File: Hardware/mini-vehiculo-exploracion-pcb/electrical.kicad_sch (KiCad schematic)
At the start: 21 parts, among them IC2 TPS564257DRLR

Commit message: actualizacion labels pcb drivers
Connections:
- net +5V renamed V_BUS
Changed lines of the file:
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@@
-	(wire
-		(pts
-			(xy 52.07 105.41) (xy 52.07 123.19)
-		)
-		(stroke
-			(width 0)
-			(type default)
-		)
-	)
 	(wire
 		(pts
@@
 	(wire
 		(pts
+			(xy 52.07 104.14) (xy 52.07 123.19)
+		)
+		(stroke
+			(width 0)
+			(type default)
+		)
+	)
+	(wire
+		(pts
 			(xy 165.1 54.61) (xy 176.53 54.61)
 		)
@@
 			(width 0)
 			(type default)
+		)
+	)
+	(global_label "V_BUS"
+		(shape input)
+		(at 52.07 104.14 0)
+		(fields_autoplaced yes)
+		(effects
+			(font
+				(size 1.27 1.27)
+			)
+			(justify left)
+		)
+		(property "Intersheetrefs" "${INTERSHEET_REFS}"
+			(at 60.9214 104.14 0)
+			(effects
+				(font
+					(size 1.27 1.27)
+				)
+				(justify left)
+				(hide yes)
+			)
 		)
 	)
@@
 					(unit 1)
 				)
-			)
-		)
-	)
-	(symbol
-		(lib_id "power:+5V")
-		(at 52.07 105.41 0)
-		(unit 1)
-		(exclude_from_sim no)
-		(in_bom yes)
-		(on_board yes)
-		(dnp no)
-		(fields_autoplaced yes)
-		(property "Reference" "#PWR024"
-			(at 52.07 109.22 0)
-			(effects
-				(font
-					(size 1.27 1.27)
-				)
-				(hide yes)
-			)
-		)
-		(property "Value" "+5V"
-			(at 52.07 100.33 0)
-			(effects
-				(font
-					(size 1.27 1.27)
-				)
-			)
-		)
-		(property "Footprint" ""
-			(at 52.07 105.41 0)
-			(effects
-				(font
-					(size 1.27 1.27)
-				)
-				(hide yes)
-			)
-		)
-		(property "Datasheet" ""
-			(at 52.07 105.41 0)
-			(effects
-				(font
-					(size 1.27 1.27)
-				)
-				(hide yes)
-			)
-		)
-		(property "Description" "Power symbol creates a global label with name \"+5V\""
-			(at 52.07 105.41 0)
-			(effects
-				(font
-					(size 1.27 1.27)
-				)
-				(hide yes)
-			)
-		)
-		(pin "1"
-		)
-		(instances
-			(project "mini-vehiculo-exploracion-pcb"
-				(path "/3cb3b833-c38f-47b4-b7e9-f0e6337b7613/d054e30f-93c7-4141-9b1f-3289ce35fefa"
-					(reference "#PWR024")
-					(unit 1)
-				)

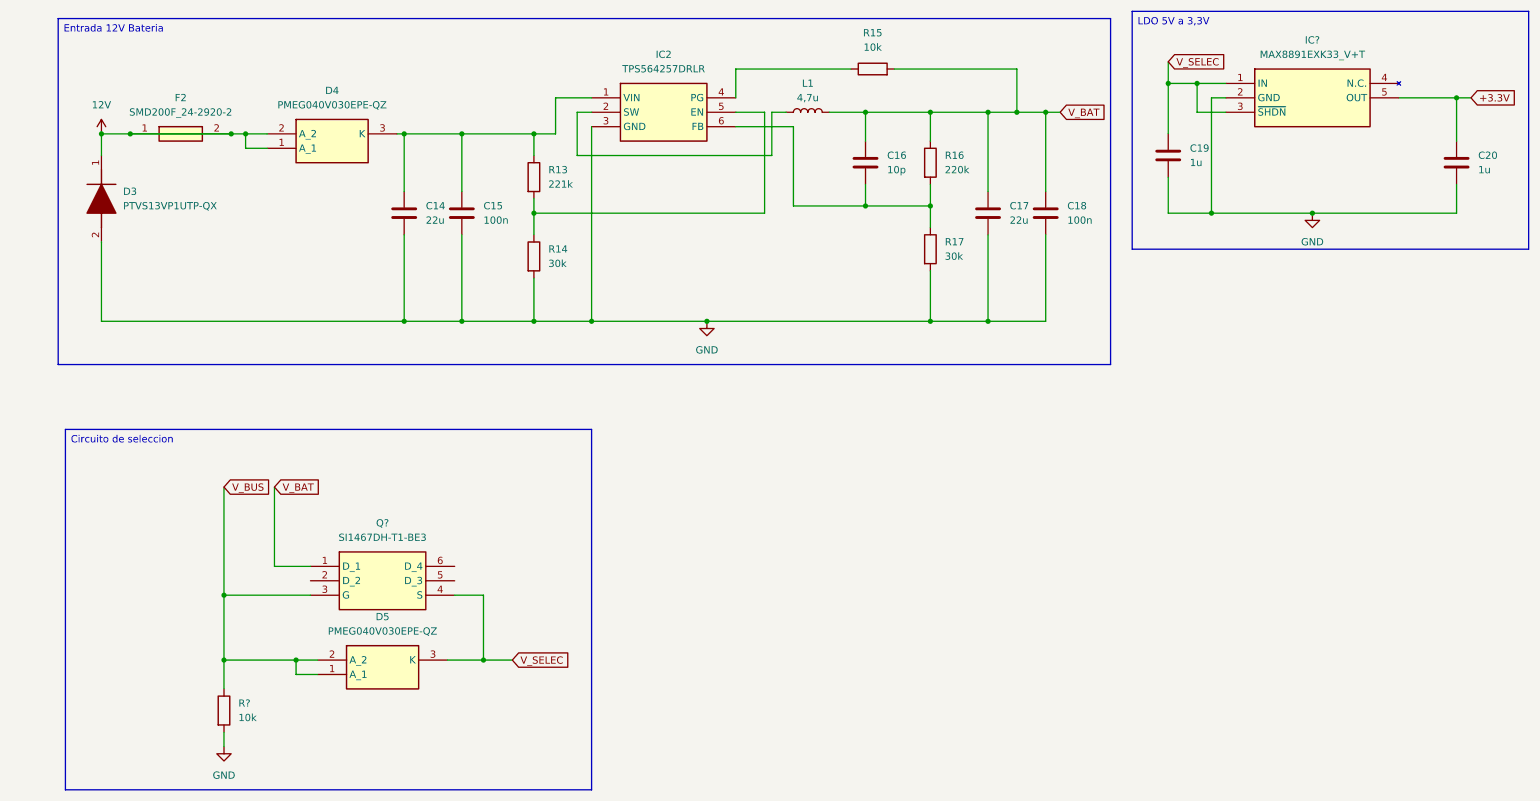
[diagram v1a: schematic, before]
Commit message: Add pin headers, run ERC
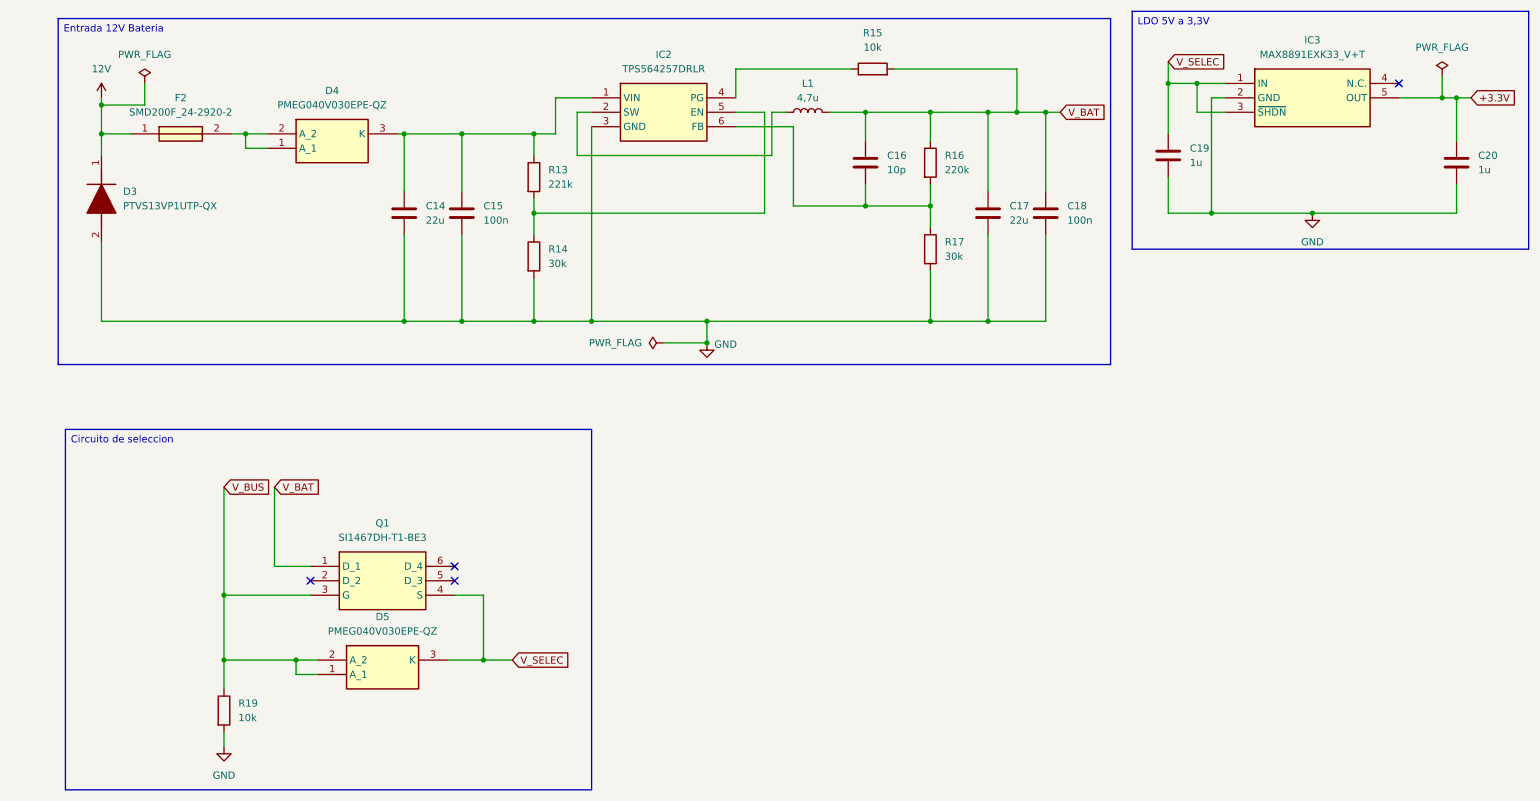
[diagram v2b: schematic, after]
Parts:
- removed R?: 10k, symbol Device:R
- added R19: 10k, symbol Device:R
- gave numbers to parts that had none: 2
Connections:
- net 12V: no longer D4.1 (A_1), D4.2 (A_2), F2.2
- net GND: now also R19.2
- net V_BUS: now also R19.1
- new net: D4.1 (A_1), D4.2 (A_2), F2.2
- no-connect marks 0 -> 4

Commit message: Assigned NET CLASSES
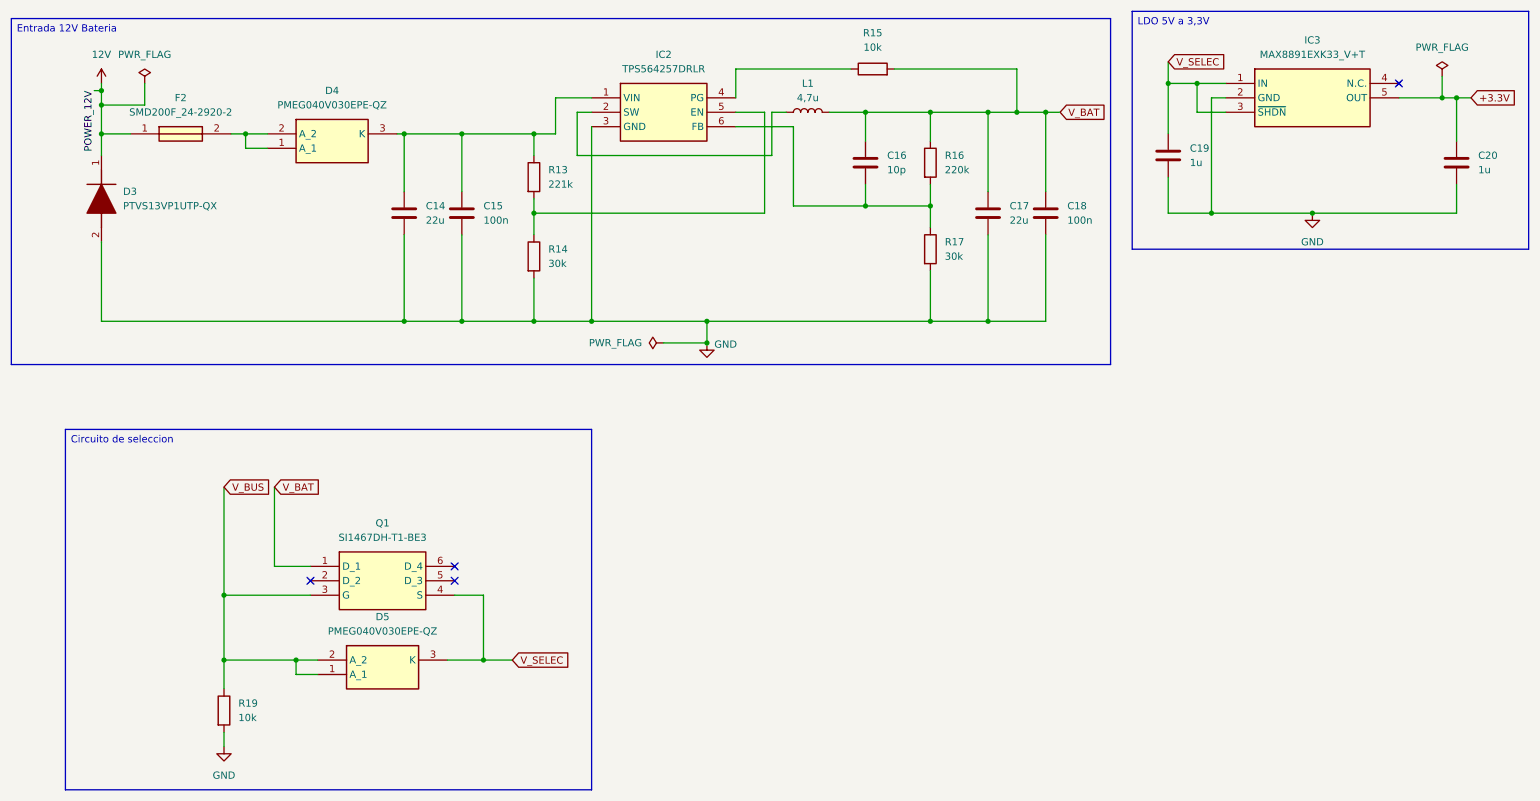
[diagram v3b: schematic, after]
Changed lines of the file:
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@@
 	(text_box "Entrada 12V Bateria\n"
 		(exclude_from_sim no)
-		(at 22.86 21.59 0)
-		(size 185.42 60.96)
+		(at 14.605 21.59 0)
+		(size 193.675 60.96)
 		(margins 0.9525 0.9525 0.9525 0.9525)
 		(stroke
@@
 	)
 	(junction
+		(at 30.48 34.29)
+		(diameter 0)
+		(color 0 0 0 0)
+	)
+	(junction
 		(at 165.1 38.1)
 		(diameter 0)
@@
 	(wire
 		(pts
+			(xy 30.48 34.29) (xy 30.48 36.83)
+		)
+		(stroke
+			(width 0)
+			(type default)
+		)
+	)
+	(wire
+		(pts
 			(xy 83.82 52.07) (xy 83.82 41.91)
 		)
@@
 	(wire
 		(pts
-			(xy 30.48 35.56) (xy 30.48 36.83)
+			(xy 30.48 33.02) (xy 30.48 34.29)
 		)
 		(stroke
@@
 	(wire
 		(pts
+			(xy 29.21 34.29) (xy 30.48 34.29)
+		)
+		(stroke
+			(width 0)
+			(type default)
+		)
+	)
+	(wire
+		(pts
 			(xy 269.24 35.56) (xy 271.78 35.56)
 		)
@@
 		)
 	)
+	(label "POWER_12V"
+		(at 29.21 34.29 270)
+		(effects
+			(font
+				(size 1.27 1.27)
+			)
+			(justify right bottom)
+		)
+	)
 	(global_label "V_BUS"
 		(shape input)
@@
 	(symbol
 		(lib_id "power:VDC")
-		(at 30.48 35.56 0)
+		(at 30.48 33.02 0)
 		(unit 1)
 		(exclude_from_sim no)
@@
 		(fields_autoplaced yes)
 		(property "Reference" "#PWR023"
-			(at 30.48 39.37 0)
+			(at 30.48 36.83 0)
 			(effects
 				(font
@@
 		)
 		(property "Value" "12V"
-			(at 30.48 30.48 0)
+			(at 30.48 27.94 0)
 			(effects
 				(font
@@
 		)
 		(property "Footprint" ""
-			(at 30.48 35.56 0)
+			(at 30.48 33.02 0)
 			(effects
 				(font
@@
 		)
 		(property "Datasheet" ""
-			(at 30.48 35.56 0)
+			(at 30.48 33.02 0)
 			(effects
 				(font
@@
 		)
 		(property "Description" "Power symbol creates a global label with name \"VDC\""
-			(at 30.48 35.56 0)
+			(at 30.48 33.02 0)
 			(effects
 				(font

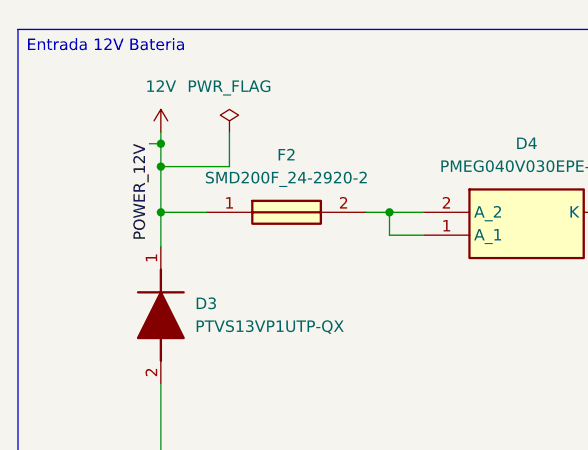
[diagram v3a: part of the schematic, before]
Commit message: Add battery sensor
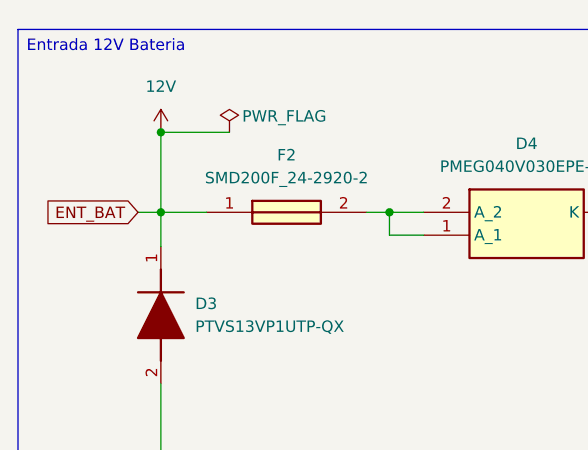
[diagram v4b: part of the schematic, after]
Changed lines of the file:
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@@
-	)
-	(junction
-		(at 30.48 34.29)
-		(diameter 0)
-		(color 0 0 0 0)
 	)
 	(junction
@@
 	)
 	(junction
-		(at 30.48 36.83)
+		(at 30.48 33.02)
 		(diameter 0)
 		(color 0 0 0 0)
@@
 	(wire
 		(pts
-			(xy 30.48 34.29) (xy 30.48 36.83)
-		)
-		(stroke
-			(width 0)
-			(type default)
-		)
-	)
-	(wire
-		(pts
 			(xy 83.82 52.07) (xy 83.82 41.91)
 		)
@@
 	(wire
 		(pts
-			(xy 38.1 33.02) (xy 38.1 36.83)
-		)
-		(stroke
-			(width 0)
-			(type default)
-		)
-	)
-	(wire
-		(pts
 			(xy 196.85 74.93) (xy 186.69 74.93)
 		)
@@
 	(wire
 		(pts
+			(xy 27.94 41.91) (xy 30.48 41.91)
+		)
+		(stroke
+			(width 0)
+			(type default)
+		)
+	)
+	(wire
+		(pts
 			(xy 110.49 41.91) (xy 106.68 41.91)
 		)
@@
 	(wire
 		(pts
-			(xy 30.48 33.02) (xy 30.48 34.29)
-		)
-		(stroke
-			(width 0)
-			(type default)
-		)
-	)
-	(wire
-		(pts
 			(xy 147.32 55.88) (xy 106.68 55.88)
 		)
@@
 	(wire
 		(pts
-			(xy 30.48 36.83) (xy 30.48 41.91)
-		)
-		(stroke
-			(width 0)
-			(type default)
-		)
-	)
-	(wire
-		(pts
 			(xy 176.53 54.61) (xy 176.53 58.42)
 		)
@@
 	(wire
 		(pts
-			(xy 29.21 34.29) (xy 30.48 34.29)
-		)
-		(stroke
-			(width 0)
-			(type default)
-		)
-	)
-	(wire
-		(pts
 			(xy 269.24 35.56) (xy 271.78 35.56)
 		)
@@
 	(wire
 		(pts
-			(xy 30.48 36.83) (xy 38.1 36.83)
+			(xy 30.48 33.02) (xy 38.1 33.02)
 		)
 		(stroke
@@
 		)
 	)
-	(label "POWER_12V"
-		(at 29.21 34.29 270)
-		(effects
-			(font
-				(size 1.27 1.27)
-			)
-			(justify right bottom)
+	(wire
+		(pts
+			(xy 30.48 33.02) (xy 30.48 41.91)
+		)
+		(stroke
+			(width 0)
+			(type default)
 		)
 	)
@@
 				)
 				(justify left)
+				(hide yes)
+			)
+		)
+	)
+	(global_label "ENT_BAT"
+		(shape input)
+		(at 27.94 41.91 180)
+		(fields_autoplaced yes)
+		(effects
+			(font
+				(size 1.27 1.27)
+			)
+			(justify right)
+		)
+		(property "Intersheetrefs" "${INTERSHEET_REFS}"
+			(at 17.2139 41.91 0)
+			(effects
+				(font
+					(size 1.27 1.27)
+				)
+				(justify right)
 				(hide yes)
 			)
@@
 		(on_board yes)
 		(dnp no)
-		(fields_autoplaced yes)
 		(property "Reference" "#FLG01"
 			(at 38.1 31.115 0)
@@
 		)
 		(property "Value" "PWR_FLAG"
-			(at 38.1 27.94 0)
-			(effects
-				(font
+			(at 44.196 31.242 0)
+			(effects
+				(font

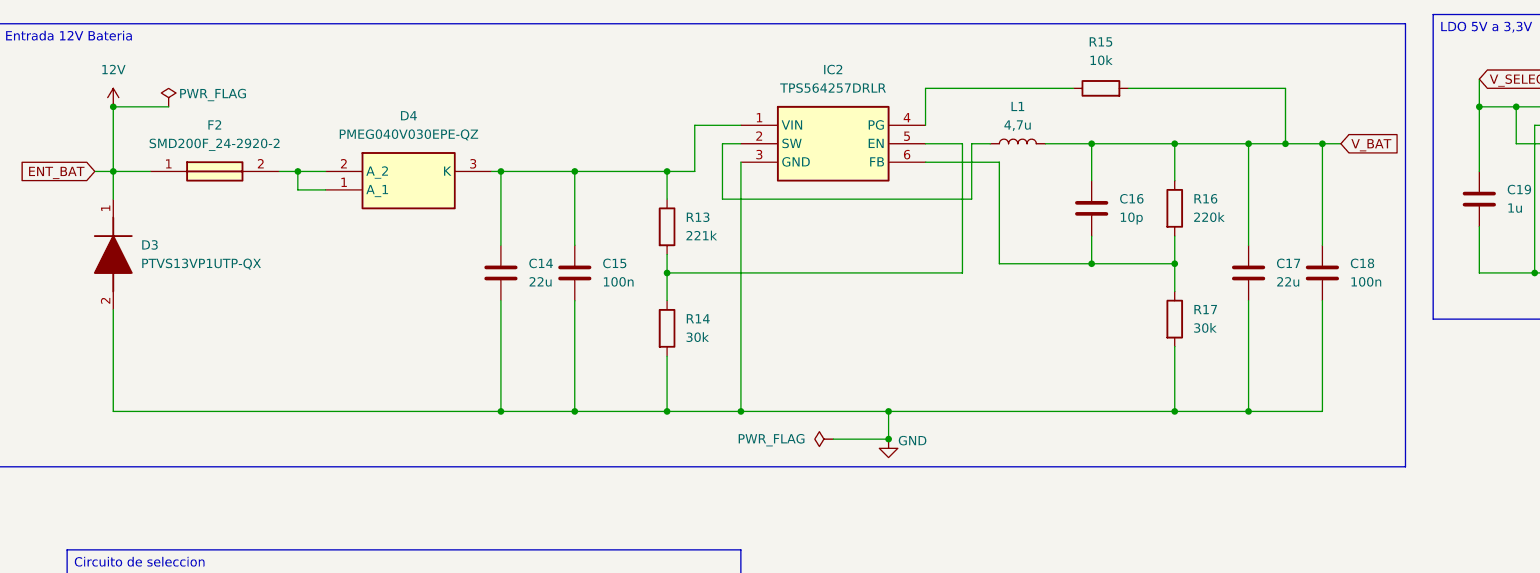
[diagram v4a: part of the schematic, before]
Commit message: cambio circuito 5V pcb control
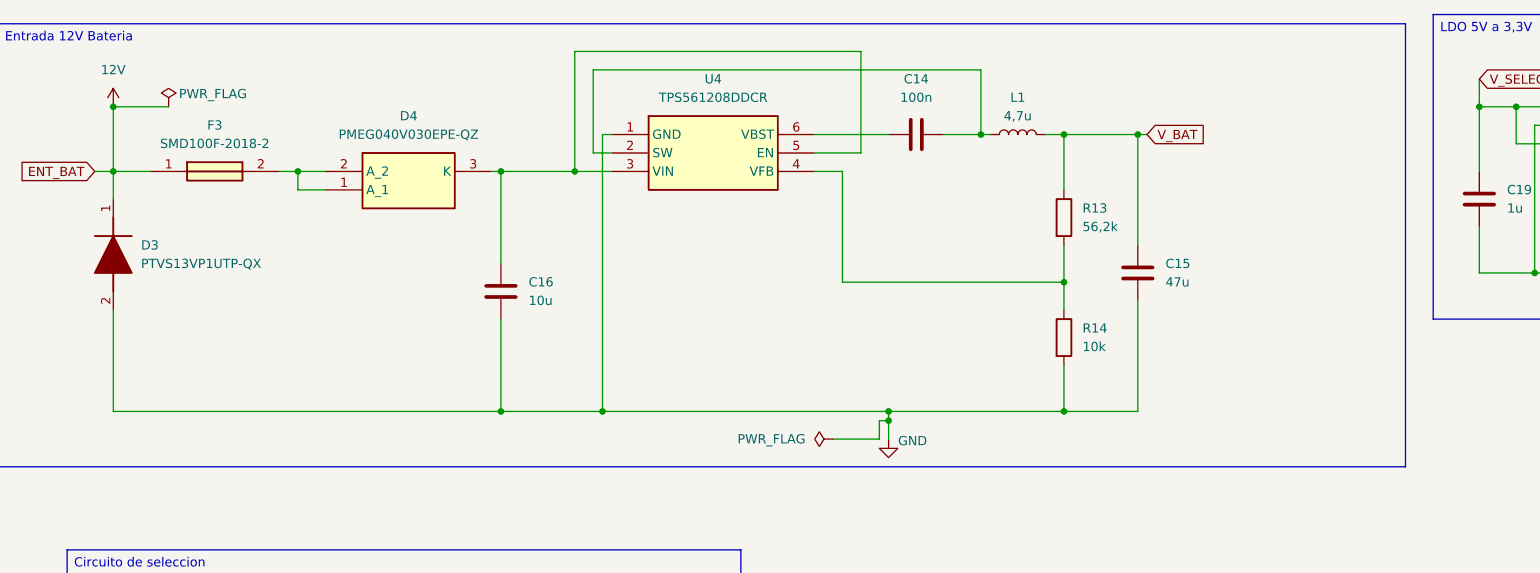
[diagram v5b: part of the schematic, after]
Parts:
- removed C17: 22u, symbol Device:C
- removed C18: 100n, symbol Device:C
- removed F2: SMD200F_24-2920-2, SMD200F2429202, symbol SMD200F_24-2920-2:SMD200F_24-2920-2
- removed IC2: TPS564257DRLR, SOTFL50P160X60-6N, symbol SamacSys_Parts:TPS564257DRLR
- removed R15: 10k, symbol Device:R
- removed R16: 220k, symbol Device:R
- removed R17: 30k, symbol Device:R
- added F3: SMD100F-2018-2, SMD030F20182, symbol SMD100F-2018-2:SMD100F-2018-2
- added U4: TPS561208DDCR, SOT95P280X110-6N, symbol TPS561208DDCR:TPS561208DDCR
- C14: value 22u -> 100n
- C15: value 100n -> 47u
- C16: value 10p -> 10u
- R13: value 221k -> 56,2k
- R14: value 30k -> 10k
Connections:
- net 12V: now also F3.1
- net GND: now also C16.2, U4.1 (GND); no longer C14.2
- net V_BAT: now also C15.1, R13.1; no longer C16.1
- net at L1.1: now also C14.2, U4.2 (SW)
- net at D4.1 (A_1), D4.2 (A_2): now also F3.2
- net at R13.2, R14.1: now also U4.4 (VFB)
- new net: C16.1, D4.3 (K), U4.3 (VIN), U4.5 (EN)
- new net: C14.1, U4.6 (VBST)

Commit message: Add footprints
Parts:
- C14, C15, C16, C19, C20: footprint (none) -> Capacitor_SMD:C_0805_2012Metric_Pad1.18x1.45mm_HandSolder
- D3: footprint SODFL4725X110N -> PTVS13VP1UTP-QX:SODFL4725X110N
- D4, D5: footprint PMEG040V030EPEQZ -> PMEG040V030EPE-QZ:PMEG040V030EPEQZ
- F3: footprint SMD030F20182 -> SMD100F-2018-2:SMD030F20182
- IC3: footprint SOT65P210X110-5N -> MAX8891EXK33_V+T:SOT65P210X110-5N
- Q1: footprint SOT65P210X110-6N -> SI1467DH-T1-BE3:SOT65P210X110-6N
- R13, R14, R19: footprint (none) -> Resistor_SMD:R_0805_2012Metric_Pad1.20x1.40mm_HandSolder
- U4: footprint SOT95P280X110-6N -> TPS561208DDCR:SOT95P280X110-6N
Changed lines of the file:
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@@
 			)
 		)
-		(property "Footprint" ""
+		(property "Footprint" "Capacitor_SMD:C_0805_2012Metric_Pad1.18x1.45mm_HandSolder"
 			(at 84.7852 62.23 0)
 			(effects
@@
 			)
 		)
-		(property "Footprint" ""
+		(property "Footprint" "Capacitor_SMD:C_0805_2012Metric_Pad1.18x1.45mm_HandSolder"
 			(at 219.4052 49.53 0)
 			(effects
@@
 			)
 		)
-		(property "Footprint" "SOT65P210X110-5N"
+		(property "Footprint" "MAX8891EXK33_V+T:SOT65P210X110-5N"
 			(at 255.27 127.94 0)
 			(effects
@@
 			)
 		)
-		(property "Footprint" "SOT95P280X110-6N"
+		(property "Footprint" "TPS561208DDCR:SOT95P280X110-6N"
 			(at 123.19 131.75 0)
 			(effects
@@
 			)
 		)
-		(property "Footprint" "PMEG040V030EPEQZ"
+		(property "Footprint" "PMEG040V030EPE-QZ:PMEG040V030EPEQZ"
 			(at 78.74 136.83 0)
 			(effects
@@
 			)
 		)
-		(property "Footprint" "SMD030F20182"
+		(property "Footprint" "SMD100F-2018-2:SMD030F20182"
 			(at 49.53 138.1 0)
 			(effects
@@
 			)
 		)
-		(property "Footprint" "PMEG040V030EPEQZ"
+		(property "Footprint" "PMEG040V030EPE-QZ:PMEG040V030EPEQZ"
 			(at 87.63 229.54 0)
 			(effects
@@
 			)
 		)
-		(property "Footprint" ""
+		(property "Footprint" "Capacitor_SMD:C_0805_2012Metric_Pad1.18x1.45mm_HandSolder"
 			(at 172.4152 59.69 0)
 			(effects
@@
 			)
 		)
-		(property "Footprint" "SODFL4725X110N"
+		(property "Footprint" "PTVS13VP1UTP-QX:SODFL4725X110N"
 			(at -66.98 57.15 0)
 			(effects
@@
 			)
 		)
-		(property "Footprint" ""
+		(property "Footprint" "Capacitor_SMD:C_0805_2012Metric_Pad1.18x1.45mm_HandSolder"
 			(at 270.2052 50.8 0)
 			(effects
@@
 			)
 		)
-		(property "Footprint" ""
+		(property "Footprint" "Capacitor_SMD:C_0805_2012Metric_Pad1.18x1.45mm_HandSolder"
 			(at 144.78 35.8648 0)
 			(effects
@@
 			)
 		)
-		(property "Footprint" "SOT65P210X110-6N"
+		(property "Footprint" "SI1467DH-T1-BE3:SOT65P210X110-6N"
 			(at 88.9 213.03 0)
 			(effects
@@
 			)
 		)
-		(property "Footprint" ""
+		(property "Footprint" "Resistor_SMD:R_0805_2012Metric_Pad1.20x1.40mm_HandSolder"
 			(at 50.292 143.51 90)
 			(effects
@@
 			)
 		)
-		(property "Footprint" ""
+		(property "Footprint" "Resistor_SMD:R_0805_2012Metric_Pad1.20x1.40mm_HandSolder"
 			(at 159.512 48.26 90)
 			(effects
@@
 			)
 		)
-		(property "Footprint" ""
+		(property "Footprint" "Resistor_SMD:R_0805_2012Metric_Pad1.20x1.40mm_HandSolder"
 			(at 159.512 64.77 90)
 			(effects
